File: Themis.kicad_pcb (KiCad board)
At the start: 2 copper layers, 100 x 50 mm, 35 parts, among them J10 Conn_01x01, J11 Conn_01x01, J12 Conn_01x01, J13 Conn_01x01, J17 SMA, J18 Conn_01x01, J20 Conn_01x01, J5 Conn_01x05, J7 SMA, J8 SMA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

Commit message: V3, work under progress, do not use as is
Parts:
- R1, R2, R3: moved to B.Cu
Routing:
- net (no net): track 3.05 -> 0.00 mm
- net Net-(J17-Pad1): track 12.1 -> 12.6 mm

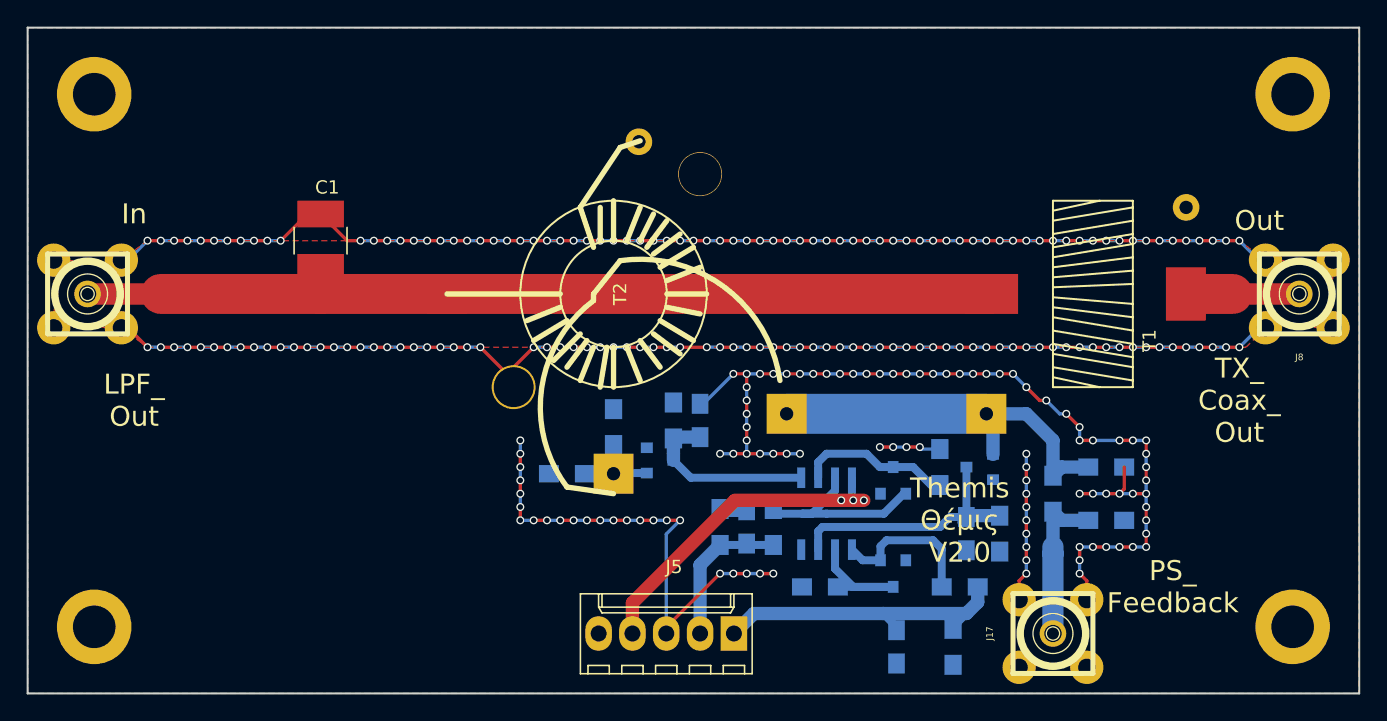
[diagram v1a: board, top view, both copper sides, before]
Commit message: V 2.1, some components switched on the bottom side
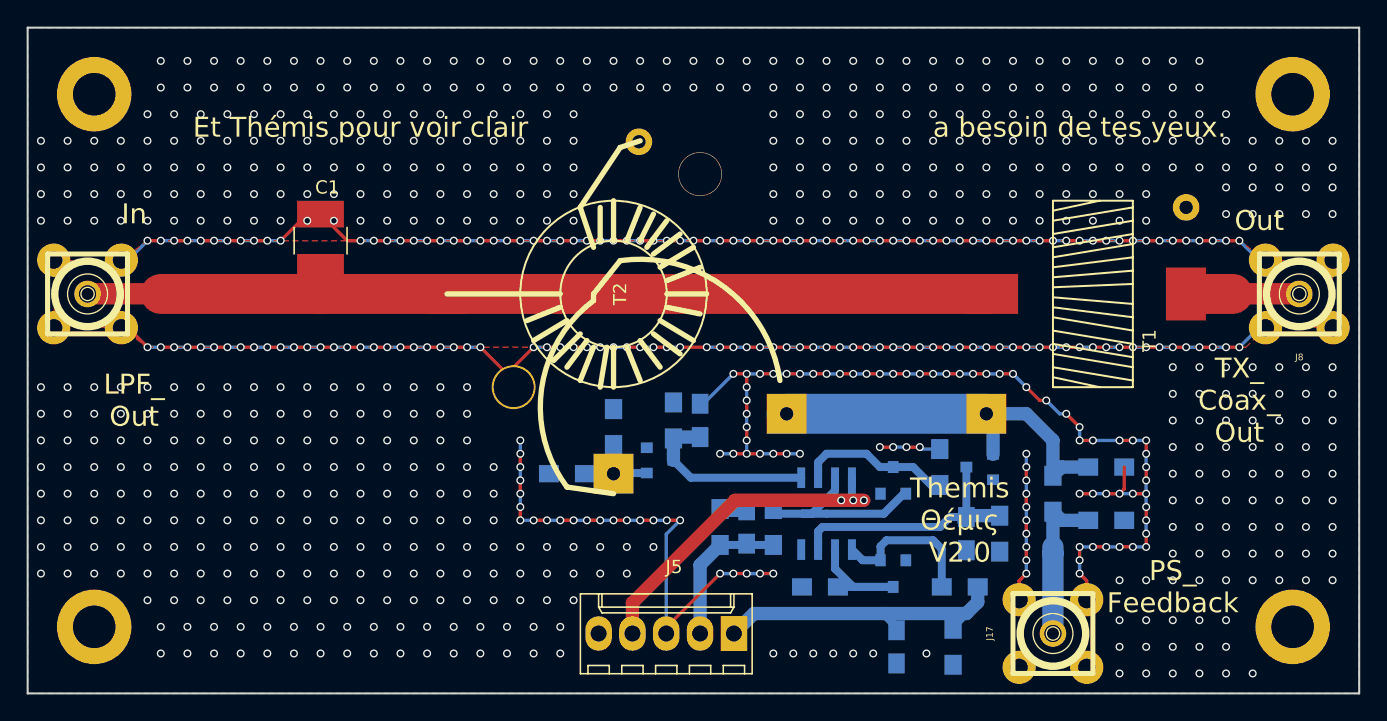
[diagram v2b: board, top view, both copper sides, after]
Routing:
- net GND: vias 258 -> 803
- net (no net): vias 0 -> 27
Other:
- board text added: "Et Thémis pour voir clair"
- board text added: "Themis Θέμις V2.1"
- board text added: "a besoin de tes yeux."

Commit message: upgrade to Kicad 5.x
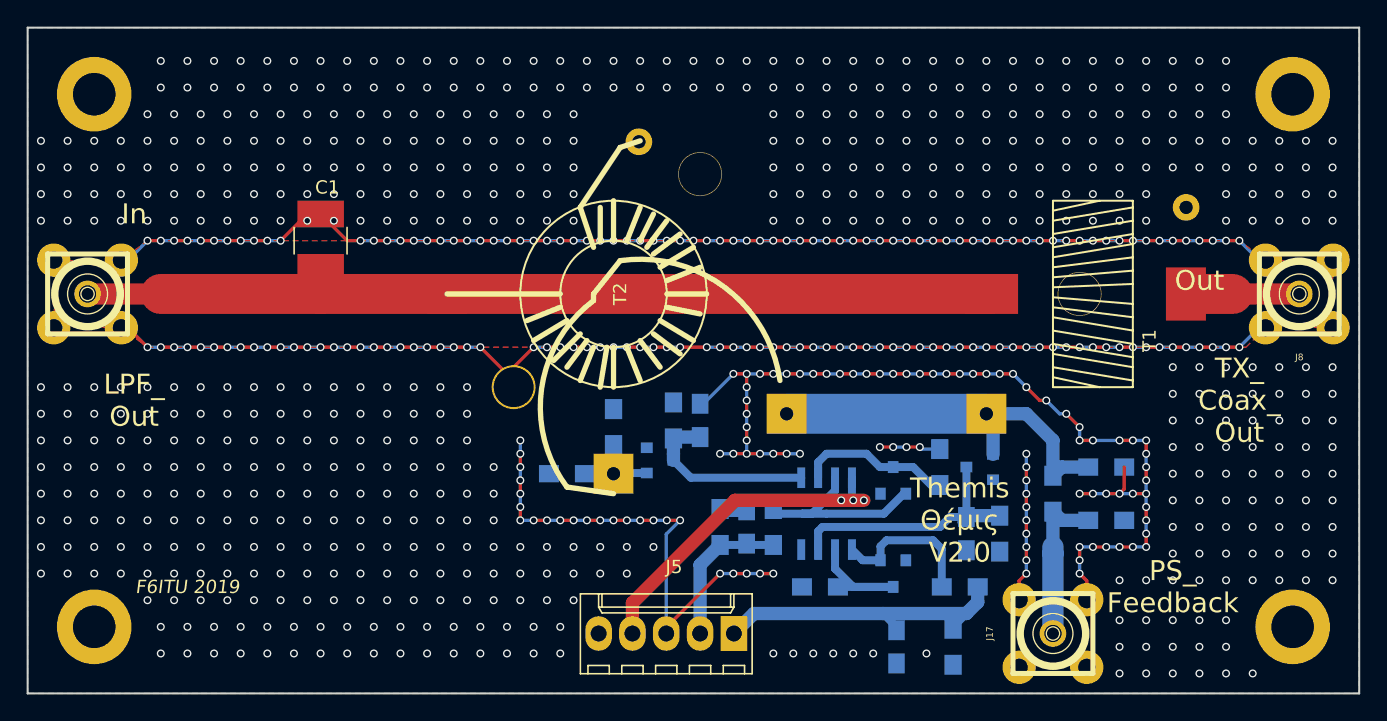
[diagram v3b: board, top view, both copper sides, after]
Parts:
- added J18: Conn_01x01, MountingHole:MountingHole_3.2mm_M3_DIN965_Pad, F.Cu at (169.0, 105.0)
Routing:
- net GND: track 308.9 -> 307.9 mm, vias 803 -> 832
- net (no net): vias 27 -> 0
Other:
- board text added: "F6ITU 2019"
- board text removed: "Et Thémis pour voir clair"
- board text removed: "a besoin de tes yeux."
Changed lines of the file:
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@@
     (thickness 1.6)
     (drawings 16)
-    (tracks 1208)
+    (tracks 1209)
     (zones 0)
-    (modules 35)
+    (modules 36)
     (nets 16)
   )
   (page A4)
   (layers
-    (0 F.Cu signal hide)
+    (0 F.Cu signal)
     (31 B.Cu signal)
     (32 B.Adhes user)
@@
     (visible_elements 7FFFFF7F)
     (pcbplotparams
-      (layerselection 0x010f0_80000001)
+      (layerselection 0x010f0_ffffffff)
       (usegerberextensions true)
       (usegerberattributes false)
       (usegerberadvancedattributes false)
       (creategerberjobfile false)
-      (excludeedgelayer true)
+      (excludeedgelayer false)
       (linewidth 0.100000)
       (plotframeref false)
@@
     (add_net "Net-(J8-Pad1)")
   )
+  (module MountingHole:MountingHole_3.2mm_M3_DIN965_Pad (layer F.Cu)
+    (at 169 105)
+    (descr "Mounting Hole 3.2mm, M3, DIN965")
+    (tags "mounting hole 3.2mm m3 din965")
+    (attr virtual)
+    (fp_text reference J18 (at 0 -3.8) (layer F.SilkS) hide
+      (effects (font (size 1 1) (thickness 0.15)))
+    )
+    (fp_text value Conn_01x01 (at 0 3.8) (layer F.Fab) hide
+      (effects (font (size 1 1) (thickness 0.15)))
+    )
+    (fp_circle (center 0 0) (end 3.05 0) (layer F.CrtYd) (width 0.05))
+    (fp_circle (center 0 0) (end 2.8 0) (layer Cmts.User) (width 0.15))
+    (fp_text user %R (at 0.3 0) (layer F.Fab)
+      (effects (font (size 1 1) (thickness 0.15)))
+    )
+    (pad 1 thru_hole circle (at 0 0) (size 3.3 3.3) (drill 3.2) (layers *.Cu *.Mask))
+  )
   (module T50:TR_T50_H_SMD (layer F.Cu)
     (at 134 105 90)
@@
     (pad 2 thru_hole circle (at -2.54 -2.54) (size 2.49936 2.49936) (drill 1.30048) (layers *.Cu *.Mask F.SilkS)
       (net 1 GND))
-    (model ../../../../../../Users/Marco/Documents/Kicad/Projets/Badge2/ndh.pretty/packages3d/SMA_Coax/SMA_PINS.wrl
+    (model C:/Users/Marco/Documents/Kicad/modules/SMA_PINS.pretty/SMA_PINS.kicad_mod
       (at (xyz 0 0 0))
       (scale (xyz 1 1 1))
@@
     )
   )
-  (gr_text "a besoin de tes yeux. " (at 169 92.5) (layer F.SilkS)
-    (effects (font (size 1.5 1.5) (thickness 0.3)))
-  )
-  (gr_text "Et Thémis pour voir clair " (at 115 92.5) (layer F.SilkS)
-    (effects (font (size 1.5 1.5) (thickness 0.3)))
+  (gr_text "F6ITU 2019" (at 102 127) (layer B.SilkS)
+    (effects (font (size 1 1) (thickness 0.25) italic) (justify mirror))
+  )
+  (gr_text "F6ITU 2019" (at 102 127) (layer F.SilkS)
+    (effects (font (size 1 1) (thickness 0.25) italic))
   )
   (gr_line (start 154 122) (end 154 89) (angle 90) (layer Eco2.User) (width 0.2))
-  (gr_text Out (at 182.5 99.5) (layer F.SilkS)
+  (gr_text Out (at 178 104) (layer F.SilkS)
     (effects (font (size 1.5 1.5) (thickness 0.3)))
   )
@@
     (effects (font (size 1.5 1.5) (thickness 0.3)) (justify mirror))
   )
-  (gr_text "\nMedium power \nDual directionnal reflectometer" (at 154 103.5) (layer B.SilkS)
+  (gr_text "\nMedium power \nDual directionnal reflectometer" (at 136.5 103.5) (layer B.SilkS)
     (effects (font (size 1.5 1.5) (thickness 0.3)) (justify mirror))
   )
@@
   (gr_line (start 190 85) (end 190 135) (angle 90) (layer Edge.Cuts) (width 0.15))
   (gr_line (start 90 85) (end 190 85) (angle 90) (layer Edge.Cuts) (width 0.15))
-  (via (at 176 95.5) (size 0.6) (drill 0.4) (layers F.Cu B.Cu) (net 0))
-  (via (at 180 91.5) (size 0.6) (drill 0.4) (layers F.Cu B.Cu) (net 0))
-  (via (at 178 91.5) (size 0.6) (drill 0.4) (layers F.Cu B.Cu) (net 0))
-  (via (at 178 93.5) (size 0.6) (drill 0.4) (layers F.Cu B.Cu) (net 0))
-  (via (at 180 95.5) (size 0.6) (drill 0.4) (layers F.Cu B.Cu) (net 0))
-  (via (at 176 93.5) (size 0.6) (drill 0.4) (layers F.Cu B.Cu) (net 0))
-  (via (at 176 91.5) (size 0.6) (drill 0.4) (layers F.Cu B.Cu) (net 0))
-  (via (at 180 93.5) (size 0.6) (drill 0.4) (layers F.Cu B.Cu) (net 0))
-  (via (at 178 95.5) (size 0.6) (drill 0.4) (layers F.Cu B.Cu) (net 0))
-  (via (at 188 93.5) (size 0.6) (drill 0.4) (layers F.Cu B.Cu) (net 0))
-  (via (at 184 93.5) (size 0.6) (drill 0.4) (layers F.Cu B.Cu) (net 0))
-  (via (at 188 95.5) (size 0.6) (drill 0.4) (layers F.Cu B.Cu) (net 0))
-  (via (at 186 93.5) (size 0.6) (drill 0.4) (layers F.Cu B.Cu) (net 0))
-  (via (at 186 95.5) (size 0.6) (drill 0.4) (layers F.Cu B.Cu) (net 0))
-  (via (at 184 95.5) (size 0.6) (drill 0.4) (layers F.Cu B.Cu) (net 0))
-  (via (at 182 95.5) (size 0.6) (drill 0.4) (layers F.Cu B.Cu) (net 0))
-  (via (at 182 93.5) (size 0.6) (drill 0.4) (layers F.Cu B.Cu) (net 0))
-  (via (at 186 97) (size 0.6) (drill 0.4) (layers F.Cu B.Cu) (net 0))
-  (via (at 182 97) (size 0.6) (drill 0.4) (layers F.Cu B.Cu) (net 0))
-  (via (at 186 99) (size 0.6) (drill 0.4) (layers F.Cu B.Cu) (net 0))
-  (via (at 184 97) (size 0.6) (drill 0.4) (layers F.Cu B.Cu) (net 0))
-  (via (at 184 99) (size 0.6) (drill 0.4) (layers F.Cu B.Cu) (net 0))
-  (via (at 182 99) (size 0.6) (drill 0.4) (layers F.Cu B.Cu) (net 0))
-  (via (at 180 99) (size 0.6) (drill 0.4) (layers F.Cu B.Cu) (net 0))
-  (via (at 180 97) (size 0.6) (drill 0.4) (layers F.Cu B.Cu) (net 0))
-  (via (at 188 97) (size 0.6) (drill 0.4) (layers F.Cu B.Cu) (net 0))
-  (via (at 188 99) (size 0.6) (drill 0.4) (layers F.Cu B.Cu) (net 0))
+  (via (at 176 91.5) (size 0.6) (drill 0.4) (layers F.Cu B.Cu) (net 1))
   (via (at 146 91.5) (size 0.6) (drill 0.4) (layers F.Cu B.Cu) (net 1))
   (via (at 105 91.5) (size 0.6) (drill 0.4) (layers F.Cu B.Cu) (net 1))
@@
   (segment (start 144 121.25) (end 142.1 121.25) (width 1) (layer B.Cu) (net 1))
   (segment (start 142.1 121.25) (end 142 121.15) (width 1) (layer B.Cu) (net 1))
-  (segment (start 140.5 95) (end 141.5 95) (width 0.25) (layer B.Cu) (net 1))
   (via (at 100 87.5) (size 0.6) (drill 0.4) (layers F.Cu B.Cu) (net 1))
   (via (at 102 87.5) (size 0.6) (drill 0.4) (layers F.Cu B.Cu) (net 1))
@@
   (via (at 153.5 132) (size 0.6) (drill 0.4) (layers F.Cu B.Cu) (net 1))
   (via (at 157.5 132) (size 0.6) (drill 0.4) (layers F.Cu B.Cu) (net 1))
+  (via (at 178 91.5) (size 0.6) (drill 0.4) (layers F.Cu B.Cu) (net 1))
+  (via (at 180 91.5) (size 0.6) (drill 0.4) (layers F.Cu B.Cu) (net 1))
+  (via (at 176 93.5) (size 0.6) (drill 0.4) (layers F.Cu B.Cu) (net 1))
+  (via (at 178 93.5) (size 0.6) (drill 0.4) (layers F.Cu B.Cu) (net 1))
+  (via (at 180 93.5) (size 0.6) (drill 0.4) (layers F.Cu B.Cu) (net 1))
+  (via (at 182 93.5) (size 0.6) (drill 0.4) (layers F.Cu B.Cu) (net 1))
+  (via (at 184 93.5) (size 0.6) (drill 0.4) (layers F.Cu B.Cu) (net 1))
+  (via (at 176 95.5) (size 0.6) (drill 0.4) (layers F.Cu B.Cu) (net 1))
+  (via (at 178 95.5) (size 0.6) (drill 0.4) (layers F.Cu B.Cu) (net 1))
+  (via (at 180 95.5) (size 0.6) (drill 0.4) (layers F.Cu B.Cu) (net 1))
+  (via (at 182 95.5) (size 0.6) (drill 0.4) (layers F.Cu B.Cu) (net 1))
+  (via (at 184 95.5) (size 0.6) (drill 0.4) (layers F.Cu B.Cu) (net 1))
+  (via (at 180 97.5) (size 0.6) (drill 0.4) (layers F.Cu B.Cu) (net 1))
+  (via (at 182 97.5) (size 0.6) (drill 0.4) (layers F.Cu B.Cu) (net 1))
+  (via (at 184 97.5) (size 0.6) (drill 0.4) (layers F.Cu B.Cu) (net 1))
+  (via (at 186 97.5) (size 0.6) (drill 0.4) (layers F.Cu B.Cu) (net 1))
+  (via (at 188 97.5) (size 0.6) (drill 0.4) (layers F.Cu B.Cu) (net 1))
+  (via (at 180 99.5) (size 0.6) (drill 0.4) (layers F.Cu B.Cu) (net 1))
+  (via (at 182 99.5) (size 0.6) (drill 0.4) (layers F.Cu B.Cu) (net 1))
+  (via (at 184 99.5) (size 0.6) (drill 0.4) (layers F.Cu B.Cu) (net 1))
+  (via (at 186 99.5) (size 0.6) (drill 0.4) (layers F.Cu B.Cu) (net 1))
+  (via (at 188 99.5) (size 0.6) (drill 0.4) (layers F.Cu B.Cu) (net 1))
+  (via (at 180 87.5) (size 0.6) (drill 0.4) (layers F.Cu B.Cu) (net 1))
+  (via (at 186 93.5) (size 0.6) (drill 0.4) (layers F.Cu B.Cu) (net 1))
+  (via (at 188 93.5) (size 0.6) (drill 0.4) (layers F.Cu B.Cu) (net 1))
+  (via (at 180 89.5) (size 0.6) (drill 0.4) (layers F.Cu B.Cu) (net 1))
+  (via (at 186 95.5) (size 0.6) (drill 0.4) (layers F.Cu B.Cu) (net 1))
+  (via (at 188 95.5) (size 0.6) (drill 0.4) (layers F.Cu B.Cu) (net 1))
   (segment (start 121.5 105) (end 114 105) (width 1) (layer F.Cu) (net 2))
   (segment (start 114 105) (end 112 103) (width 1) (layer F.Cu) (net 2))
@@
     (polygon
       (pts
-        (xy 95 130.5) (xy 153 130.5) (xy 153 121.5) (xy 153.4 121.5) (xy 153.4 120.5)
-        (xy 153 120.5) (xy 153 109.5) (xy 98 109.5) (xy 95 106.5)
+        (xy 95 130.5) (xy 153 130.5) (xy 153 121.5) (xy 153.5 121) (xy 153.5 120)
+        (xy 153 119.5) (xy 153 109.5) (xy 98 109.5) (xy 95 106.5)
       )
     )
